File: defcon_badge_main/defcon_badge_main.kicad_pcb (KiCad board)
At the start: 4 copper layers, 103.5 x 89.6 mm, 131 parts, among them M1 Motor 1, M2 Motor 2, M3 Motor 3, U3 ESP32-C5-WROOM-1U, U5 DRIVER-A4988SETTR-T_QFN28_, U6 DRIVER-A4988SETTR-T_QFN28_, U8 DRIVER-A4988SETTR-T_QFN28_

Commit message: added component parts and modifications
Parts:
- removed J_LIM4, J_LIM5, J_LIM6: Conn_01x02_Pin, joystick:pad_limit_switch
- C1_EN1, C2_DC3, C_BOOT1, C_LIM1, R1_EN1: footprint joystick:R_0805_2012Metric_Pad1.20x1.40mm_HandSolder_MINE -> joystick:R_0603_1608Metric_Pad0.98x0.95mm_HandSolder_MINE
- C2_V8: footprint joystick:R_0402_1005Metric_Pad0.72x0.64mm_HandSolder_MINE -> joystick:R_0603_1608Metric_Pad0.98x0.95mm_HandSolder_MINE
- C_MENU1: footprint joystick:R_0805_2012Metric_Pad1.20x1.40mm_HandSolder_MINE -> joystick:R_0402_1005Metric_Pad0.72x0.64mm_HandSolder_MINE
- Q_BLED1, Q_GLED1, Q_RLED1: footprint joystick:npn -> joystick:SOT-23-3
- R1_LIM1: value 10 kOhm -> 10 kOhm; footprint joystick:R_1206_3216Metric_Pad1.30x1.75mm_HandSolder_MINE -> joystick:R_0805_2012Metric_Pad1.20x1.40mm_HandSolder_MINE
- R_MENU1: value 10k Ohm -> 10 kOhm
- R_SNS1_M1, R_SNS1_M2, R_SNS1_M3, R_SNS2_M1, R_SNS2_M2, R_SNS2_M3: value 1ohm -> 1 Ohm
- moved Q_BLED1 1.92 mm to (-16.8, -38.3), turned to 0 degrees
- moved Q_RLED1 1.58 mm to (-21.9, -35.5)
- moved Q_GLED1 1.44 mm to (-21.0, -30.6), turned to 90 degrees
- moved R2_CS_M3 0.50 mm to (5.80, 19.8)
- moved R2_BLED1 0.50 mm to (-13.4, -40.1)
- moved J_LIM1 0.46 mm to (8.70, -11.9)
- moved R2_CS_M1 0.30 mm to (-14.4, 20.9)
- moved J_LIM2 0.24 mm to (9.90, -9.85)
- moved R2_CS_M2 0.05 mm to (22.3, 21.2)
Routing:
- net /limit_switch/SW_PARALLEL: track 11.4 -> 20.9 mm
- net /esp32/USB_D_P: track 19.6 -> 25.2 mm
- net /STEPPER_3_STEP: track 76.0 -> 72.4 mm
- net /led/LED_G_SIG: track 10.2 -> 13.3 mm
- net /STEPPER_3_DIR: track 70.0 -> 66.9 mm
- net /led/LED_B_SIG: track 2.00 -> 5.01 mm
- net /led/LED_R_POW: track 2.85 -> 5.16 mm
- net /STEPPER_1_DIR: track 63.6 -> 61.4 mm
- net /STEPPER_1_STEP: track 63.5 -> 65.4 mm
- net Net-(RED_1-Pin_1): track 285.1 -> 283.3 mm
- net /led/LED_B_POW: track 4.09 -> 2.50 mm
- net /STEPPER_2_STEP: track 70.9 -> 69.9 mm
- net /led/LED_G_POW: track 2.04 -> 3.02 mm
- net /STEPPER_MS3: track 151.9 -> 152.7 mm
- net /led/LED_R_SIG: track 2.97 -> 2.32 mm
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- removed copper zone on F.Cu, net /limit_switch/SW_PARALLEL

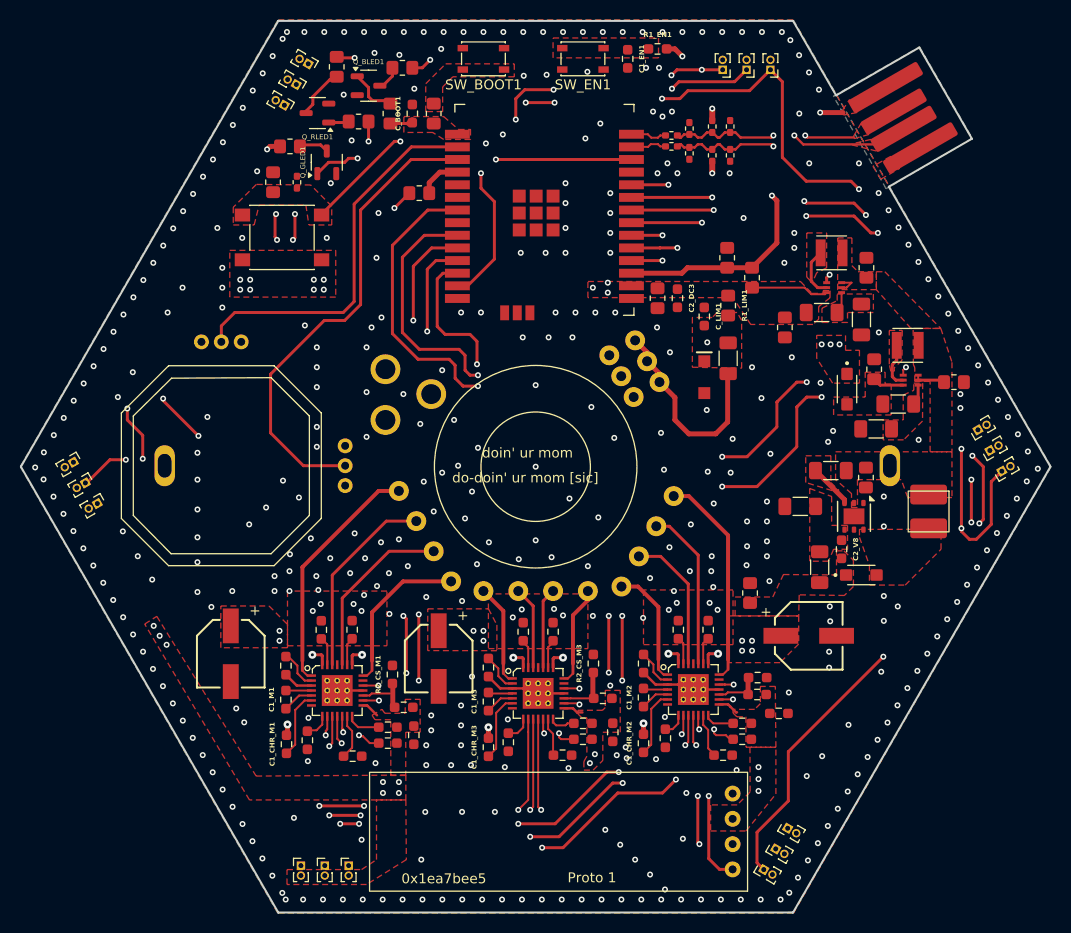
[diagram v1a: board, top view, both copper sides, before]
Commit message: Started adding software
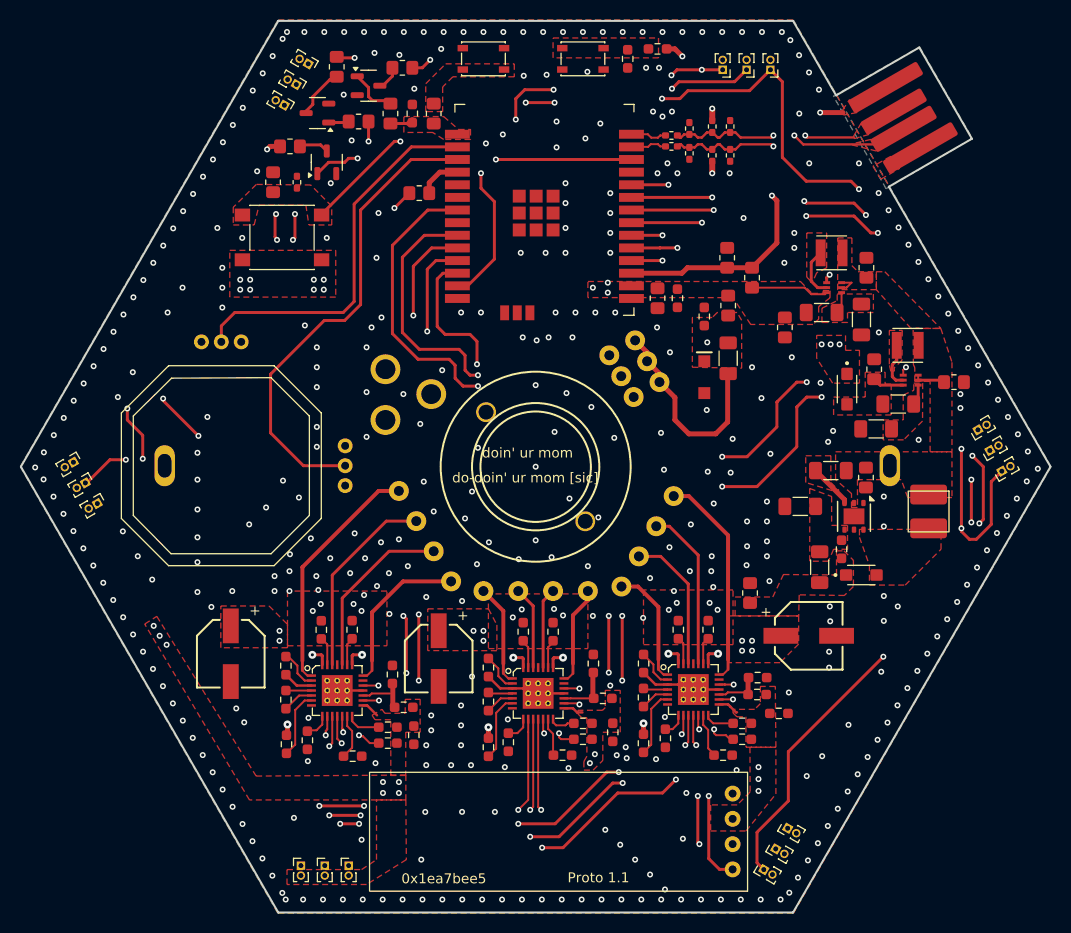
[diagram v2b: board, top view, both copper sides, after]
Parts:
- added REF**: motor_mount, joystick:motor_mount, F.Cu at (0.00, 0.00)
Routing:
- net /STEPPER_1_STEP: track 65.4 -> 68.7 mm
- net /STEPPER_1_DIR: track 61.4 -> 63.5 mm
- net /STEPPER_MS2: track 156.6 -> 155.3 mm
- net /STEPPER_MS3: track 152.7 -> 151.5 mm
- net /STEPPER_MS1: track 154.4 -> 153.2 mm
- net GND: vias 386 -> 388
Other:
- board text added: "Proto 1.1"
- board text removed: "Proto 1"
